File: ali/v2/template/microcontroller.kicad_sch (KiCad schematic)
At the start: 39 parts, among them J1 Conn_02x01, J2 Conn_01x05, J3 USB_C_Receptacle_USB2.0_16P, J6 Screw_Terminal_01x02, SW1 SKRPANE010, U1 STM32H563RIV6, U2 AP2112K-3.3, Y1 25 MHz

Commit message: mfw LCs
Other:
- note added: "GPIO"
- note added: "POWER"
- note removed: "GPIO Banks"
- moved on the sheet: C1, C10, C11, C2, C3, C4, C5, C6, C7, C8, C9, D1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

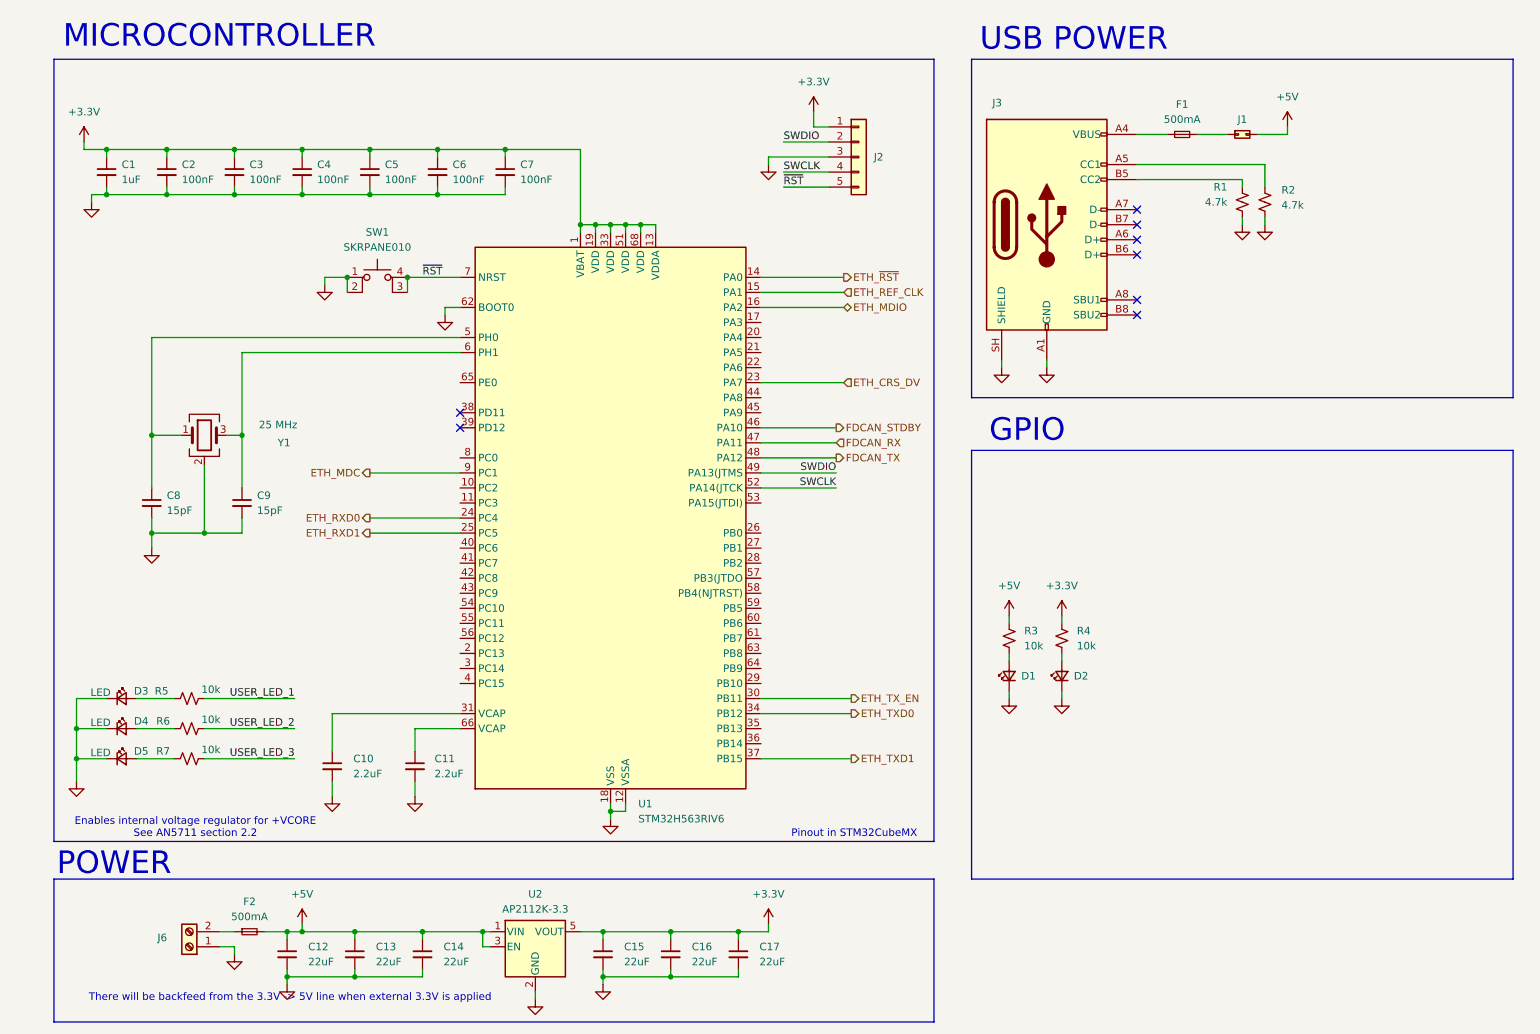
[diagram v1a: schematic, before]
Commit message: the great flatpak and kicad 10.0.6 migration
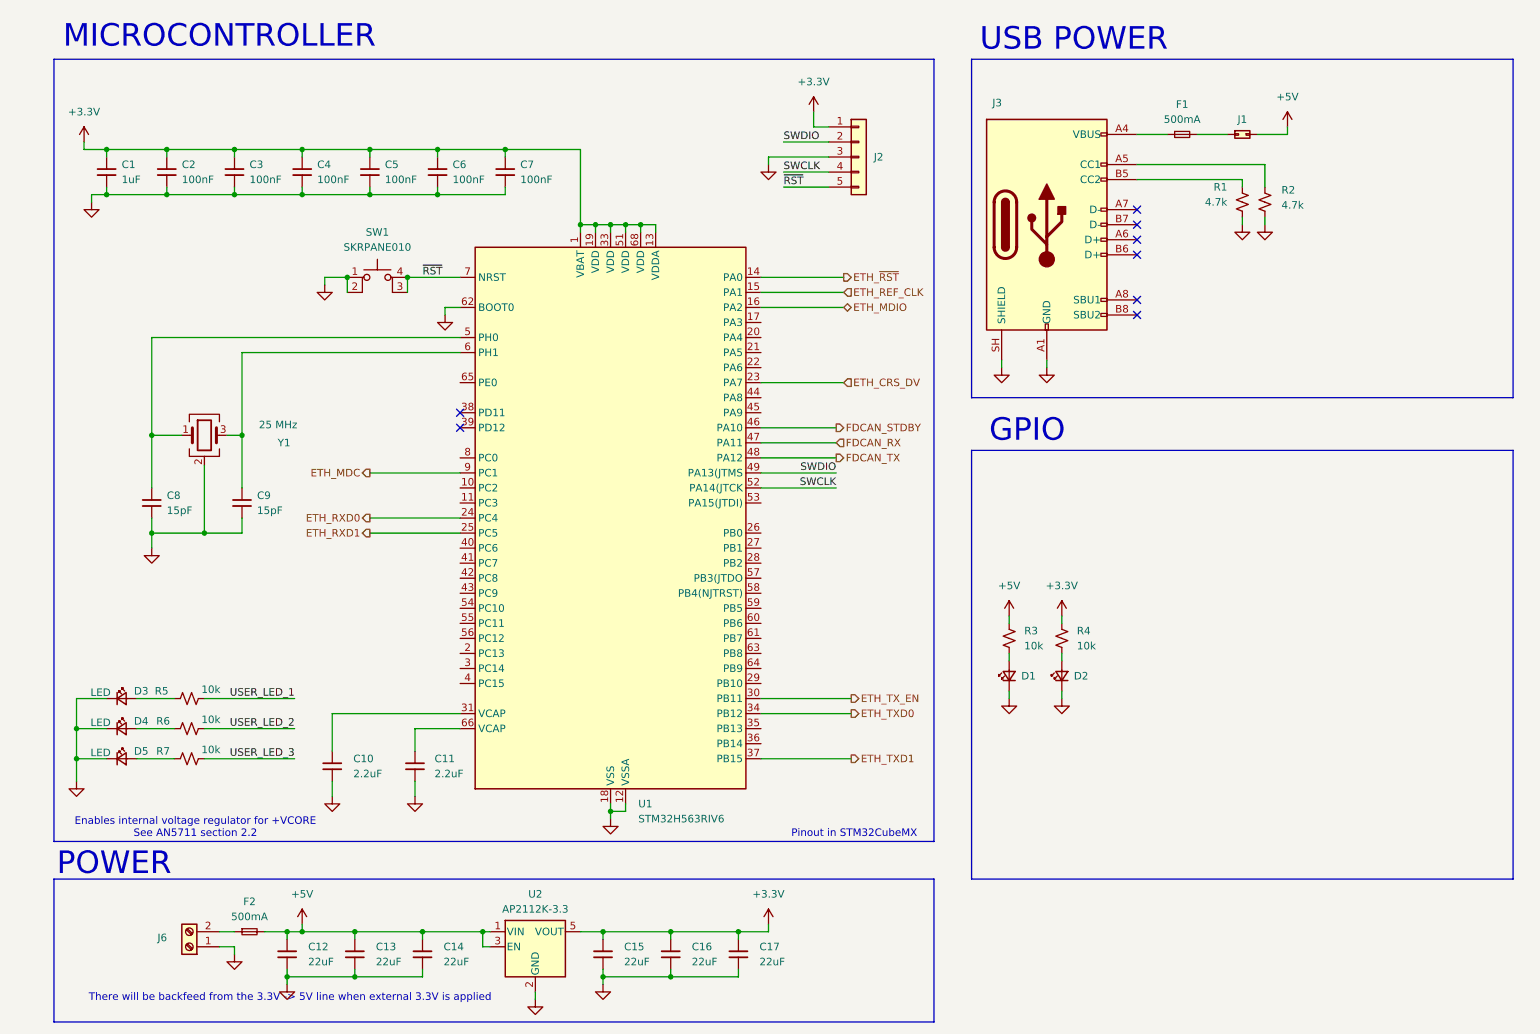
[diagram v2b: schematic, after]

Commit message: The other half of the great 10.0.6 migration
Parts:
- U1: symbol MCU_ST_STM32H5:STM32H563RIVx -> APRL_MCU:STM32H563RIVx
